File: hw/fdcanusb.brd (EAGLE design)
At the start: 41 x 32 mm, 37 parts, among them J1 MF-CON-MICROUSB-RIGHT, J3 JST-ZH6SMT_VERT, M1 MOUNT, M2 MOUNT, M3 MOUNT, M4 MOUNT, U1 MF-REG-SOT235-3.3V-300mA, U2 USBLC6-2SC6, U3 TCAN334GSOT23, U4 TLP3317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

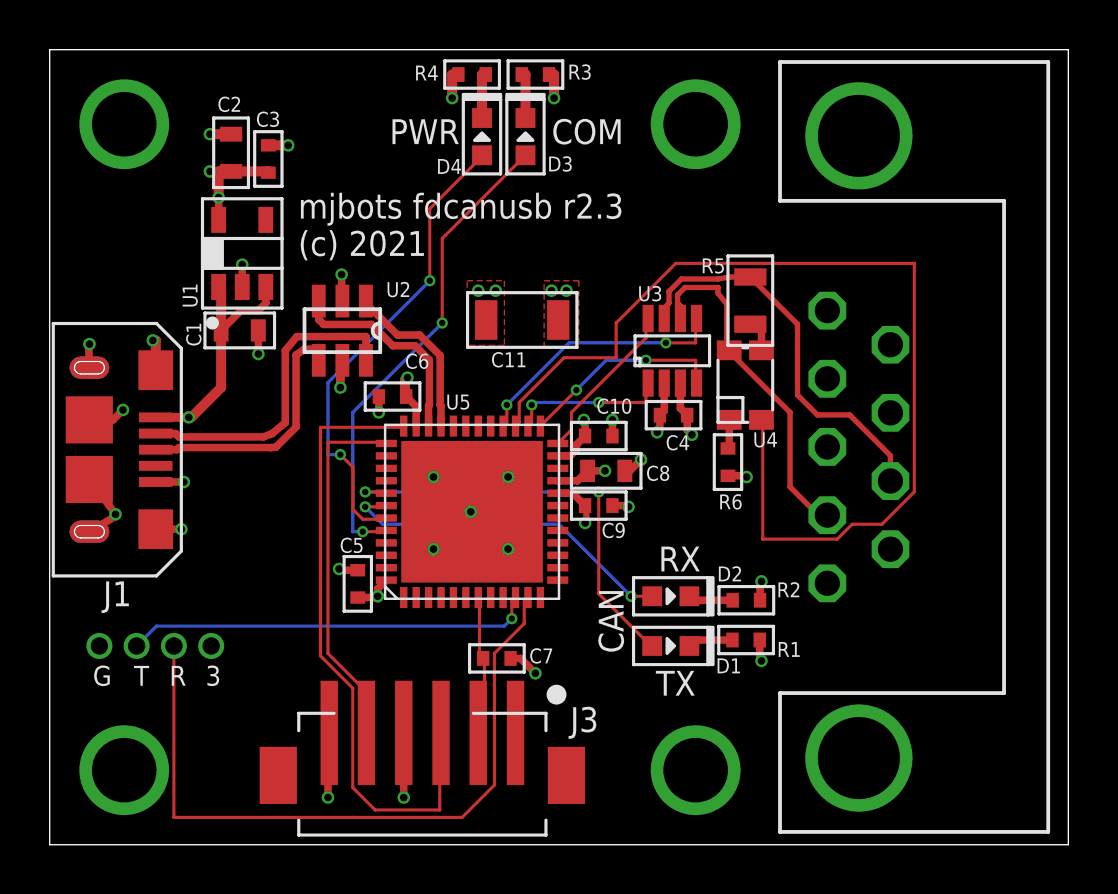
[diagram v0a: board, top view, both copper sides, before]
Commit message: Update PCB to fdcanusb r2.4  * All components are increased to minimum 0603  * Switch to the SOIC package for the CAN transceiver, which is easier    to get  * Switch to 6mil min space/trace
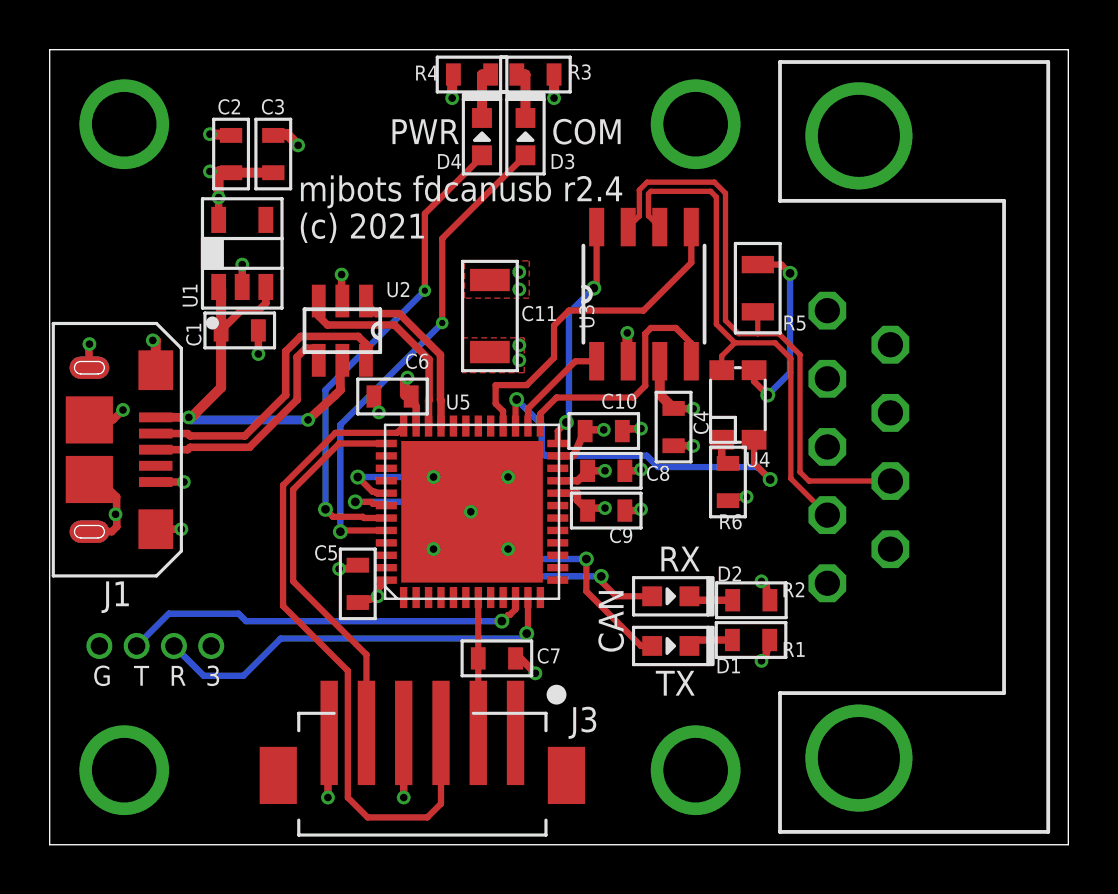
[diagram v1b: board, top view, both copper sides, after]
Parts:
- C10, C3, C4, C5, C6, C7, C9: device mfpassives:C0402 -> mfpassives:C0603
- R1, R2, R3, R4, R6: device mfpassives:R0402 -> mfpassives:R0603
- R5: value 100 -> 120
- U3: value TCAN334GSOT23 -> TCAN334G; device fdcanusb:SOT23-8 -> fdcanusb:SOIC8
- moved U3 2.55 mm to (23.9, 22.2), turned to 90 degrees
- moved C11 1.31 mm to (17.7, 21.3), turned to 90 degrees
- moved U4 0.85 mm to (27.7, 17.7)
- moved R6 0.80 mm to (27.3, 14.6)
- moved R5 0.58 mm to (28.5, 22.4), turned to 90 degrees
- moved C4 0.48 mm to (25.1, 16.8), turned to 270 degrees
- moved C9 0.36 mm to (22.4, 13.4)
- moved C10 0.28 mm to (22.3, 16.6)
- moved C3 0.28 mm to (9.00, 27.8)
- moved R1 0.20 mm to (28.2, 8.24)
- moved R2 0.20 mm to (28.2, 9.84)
- moved C2 0.05 mm to (7.30, 27.8)
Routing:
- net CAN_TERM: track 41.0 -> 15.1 mm, vias 0 -> 2
- net DEBUG_RX: track 28.4 -> 16.9 mm, vias 0 -> 1
- net CAN_P: track 16.0 -> 23.5 mm
- net CAN_N: track 14.0 -> 21.3 mm
- net N$7: track 1.45 -> 7.95 mm, vias 0 -> 2
- net CAN_SHDN: track 10.5 -> 13.9 mm, vias 2 -> 0
- net CAN_STB: track 6.54 -> 9.36 mm, vias 0 -> 2
- net CAN_TX: track 6.37 -> 4.26 mm, vias 2 -> 0
- net CAN_RX: track 8.29 -> 10.2 mm, vias 2 -> 0
- net +3V3: track 20.8 -> 22.2 mm
- net SWDIO: track 25.4 -> 26.7 mm
- net LED_CAN_RX: track 13.9 -> 15.0 mm
- net USB_D_N: track 12.8 -> 12.0 mm
- net SWCLK: track 14.7 -> 15.5 mm
- net LED_COM: track 19.4 -> 20.1 mm
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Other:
- board text added: "mjbots fdcanusb r2.4 (c) 2021"
- board text removed: "mjbots fdcanusb r2.3 (c) 2021"

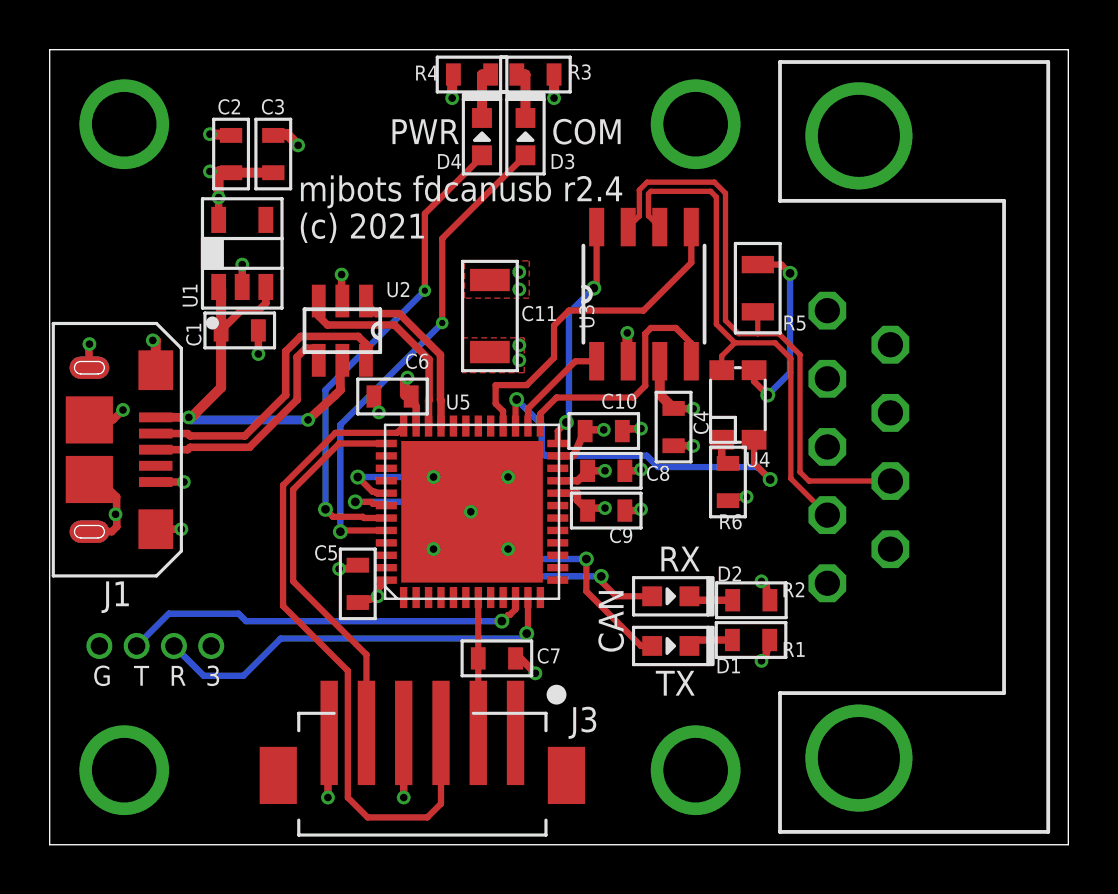
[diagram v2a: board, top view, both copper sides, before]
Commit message: Fine silk placement
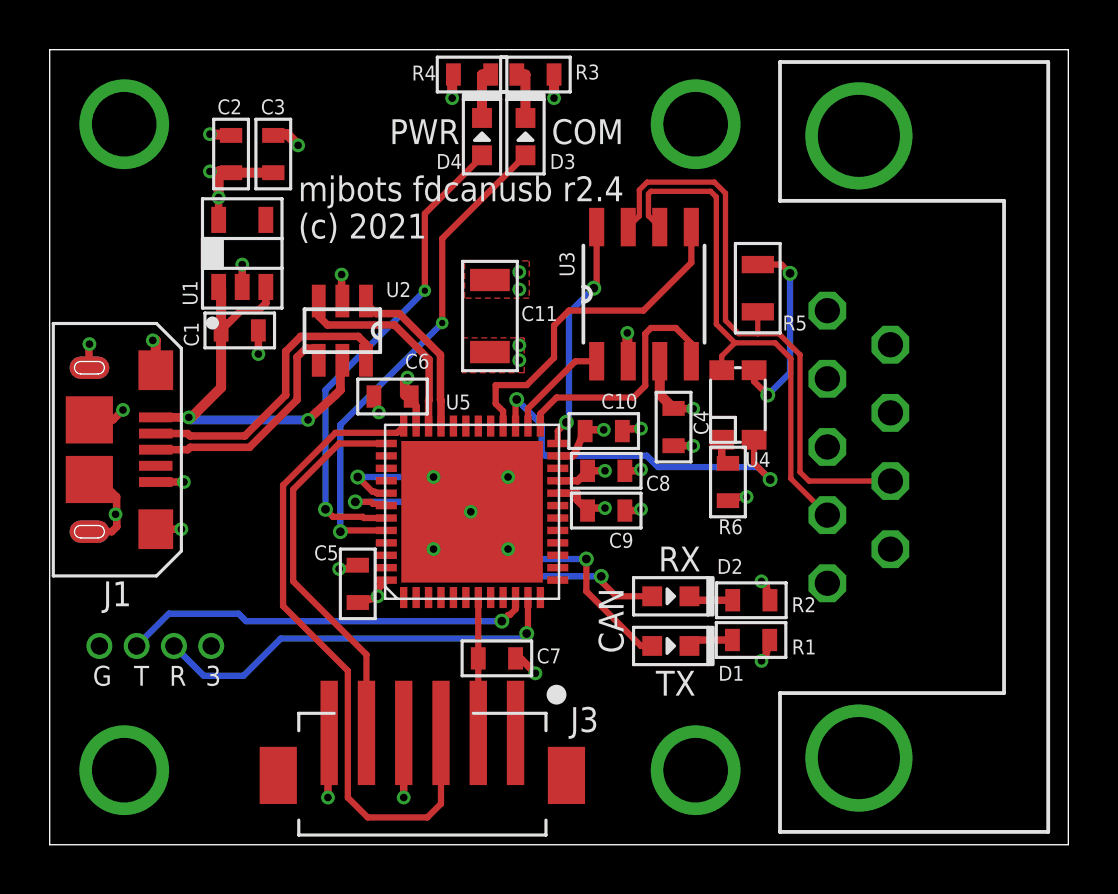
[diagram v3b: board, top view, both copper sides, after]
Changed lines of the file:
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@@
 <attribute name="HOUSEPART" value="YES" x="63.63" y="39.04" size="1.778" layer="27" rot="R90" display="off"/>
 <attribute name="MPN" value="MF-REG-SOT235-3.3V-300mA" x="63.63" y="39.04" size="1.778" layer="27" rot="R90" display="off"/>
-<attribute name="NAME" x="5.95" y="21.6" size="0.6" layer="25" font="vector" ratio="10" rot="R90"/>
+<attribute name="NAME" x="5.95" y="21.7" size="0.6" layer="25" font="vector" ratio="10" rot="R90"/>
 <attribute name="POPULATE" value="1" x="63.63" y="39.04" size="1.778" layer="27" rot="R90" display="off"/>
 <attribute name="URL" value="https://factory.macrofab.com/part/MF-REG-SOT235-3.3V-300mA" x="63.63" y="39.04" size="1.778" layer="27" rot="R90" display="off"/>
@@
 <attribute name="HOUSEPART" value="YES" x="22.89" y="-40.26" size="1.778" layer="27" display="off"/>
 <attribute name="MPN" value="MF-CAP-0603-1uF" x="22.89" y="-40.26" size="1.778" layer="27" display="off"/>
-<attribute name="NAME" x="6.1" y="20.05" size="0.6" layer="25" font="vector" ratio="10" rot="R90"/>
+<attribute name="NAME" x="6" y="20.05" size="0.6" layer="25" font="vector" ratio="10" rot="R90"/>
 <attribute name="POPULATE" value="1" x="22.89" y="-40.26" size="1.778" layer="27" display="off"/>
 <attribute name="TOLERANCE" value="" x="22.89" y="-40.26" size="1.778" layer="27" display="off"/>
@@
 <attribute name="MF" value="TI" x="23.92" y="22.16" size="1.778" layer="27" rot="R90" display="off"/>
 <attribute name="MPN" value="TCAN330GDR" x="23.92" y="22.16" size="1.778" layer="27" rot="R90" display="off"/>
-<attribute name="NAME" x="21.92" y="20.76" size="0.6" layer="25" font="vector" ratio="10" rot="R90"/>
+<attribute name="NAME" x="21.12" y="22.86" size="0.6" layer="25" font="vector" ratio="10" rot="R90"/>
 <attribute name="POPULATE" value="1" x="23.92" y="22.16" size="1.778" layer="27" rot="R90" display="off"/>
 </element>
@@
 <attribute name="HOUSEPART" value="YES" x="68.12" y="-47.51" size="1.778" layer="27" display="off"/>
 <attribute name="MPN" value="MF-CAP-0603-0.1uF" x="68.12" y="-47.51" size="1.778" layer="27" display="off"/>
-<attribute name="NAME" x="23.5" y="12.75" size="0.6" layer="25" font="vector" ratio="10" rot="R180"/>
+<attribute name="NAME" x="23.5" y="12.55" size="0.6" layer="25" font="vector" ratio="10" rot="R180"/>
 <attribute name="POPULATE" value="1" x="68.12" y="-47.51" size="1.778" layer="27" display="off"/>
 <attribute name="TOLERANCE" value="" x="68.12" y="-47.51" size="1.778" layer="27" display="off"/>
@@
 <attribute name="HOUSEPART" value="YES" x="45.26" y="-45.91" size="1.778" layer="27" display="off"/>
 <attribute name="MPN" value="MF-CAP-0603-1uF" x="45.26" y="-45.91" size="1.778" layer="27" display="off"/>
-<attribute name="NAME" x="24" y="14.65" size="0.6" layer="25" font="vector" ratio="10"/>
+<attribute name="NAME" x="24" y="14.25" size="0.6" layer="25" font="vector" ratio="10"/>
 <attribute name="POPULATE" value="1" x="45.26" y="-45.91" size="1.778" layer="27" display="off"/>
 <attribute name="TOLERANCE" value="" x="45.26" y="-45.91" size="1.778" layer="27" display="off"/>
@@
 <attribute name="HOUSEPART" value="YES" x="-13.1" y="62.61" size="1.778" layer="27" rot="R180" display="off"/>
 <attribute name="MPN" value="MF-LED-0603-GREEN" x="-13.1" y="62.61" size="1.778" layer="27" rot="R180" display="off"/>
-<attribute name="NAME" x="26.81" y="6.9" size="0.6" layer="25" font="vector" ratio="10"/>
+<attribute name="NAME" x="26.91" y="6.6" size="0.6" layer="25" font="vector" ratio="10"/>
 <attribute name="POPULATE" value="1" x="-13.1" y="62.61" size="1.778" layer="27" rot="R180" display="off"/>
 <attribute name="URL" value="https://factory.macrofab.com/part/MF-LED-0603-GREEN" x="-13.1" y="62.61" size="1.778" layer="27" rot="R180" display="off"/>
@@
 <attribute name="HOUSEPART" value="YES" x="-20.72" y="64.61" size="1.778" layer="27" rot="R180" display="off"/>
 <attribute name="MPN" value="MF-LED-0603-RED" x="-20.72" y="64.61" size="1.778" layer="27" rot="R180" display="off"/>
-<attribute name="NAME" x="26.86" y="10.6" size="0.6" layer="25" font="vector" ratio="10"/>
+<attribute name="NAME" x="26.86" y="10.9" size="0.6" layer="25" font="vector" ratio="10"/>
 <attribute name="POPULATE" value="1" x="-20.72" y="64.61" size="1.778" layer="27" rot="R180" display="off"/>
 <attribute name="URL" value="https://factory.macrofab.com/part/MF-LED-0603-RED" x="-20.72" y="64.61" size="1.778" layer="27" rot="R180" display="off"/>
@@
 <attribute name="HOUSEPART" value="YES" x="-21.3" y="69.2" size="1.778" layer="27" rot="R180" display="off"/>
 <attribute name="MPN" value="MF-RES-0603-220" x="-21.3" y="69.2" size="1.778" layer="27" rot="R180" display="off"/>
-<attribute name="NAME" x="29.47" y="7.56" size="0.6" layer="25" font="vector" ratio="10"/>
+<attribute name="NAME" x="29.87" y="7.66" size="0.6" layer="25" font="vector" ratio="10"/>
 <attribute name="POPULATE" value="1" x="-21.3" y="69.2" size="1.778" layer="27" rot="R180" display="off"/>
 <attribute name="TOLERANCE" value="" x="-21.3" y="69.2" size="1.778" layer="27" rot="R180" display="off"/>
@@
 <attribute name="HOUSEPART" value="YES" x="-25.1" y="70.8" size="1.778" layer="27" rot="R180" display="off"/>
 <attribute name="MPN" value="MF-RES-0603-220" x="-25.1" y="70.8" size="1.778" layer="27" rot="R180" display="off"/>
-<attribute name="NAME" x="29.46" y="9.96" size="0.6" layer="25" font="vector" ratio="10"/>
+<attribute name="NAME" x="29.86" y="9.36" size="0.6" layer="25" font="vector" ratio="10"/>
 <attribute name="POPULATE" value="1" x="-25.1" y="70.8" size="1.778" layer="27" rot="R180" display="off"/>
 <attribute name="TOLERANCE" value="" x="-25.1" y="70.8" size="1.778" layer="27" rot="R180" display="off"/>
@@
 <attribute name="HOUSEPART" value="YES" x="5.58" y="95.77" size="1.778" layer="27" rot="R180" display="off"/>
 <attribute name="MPN" value="MF-RES-0603-220" x="5.58" y="95.77" size="1.778" layer="27" rot="R180" display="off"/>
-<attribute name="NAME" x="20.85" y="30.8" size="0.6" layer="25" font="vector" ratio="10"/>
+<attribute name="NAME" x="21.15" y="30.8" size="0.6" layer="25" font="vector" ratio="10"/>
 <attribute name="POPULATE" value="1" x="5.58" y="95.77" size="1.778" layer="27" rot="R180" display="off"/>
 <attribute name="TOLERANCE" value="" x="5.58" y="95.77" size="1.778" layer="27" rot="R180" display="off"/>
@@
 <attribute name="HOUSEPART" value="YES" x="34.78" y="-33.77" size="1.778" layer="27" display="off"/>
 <attribute name="MPN" value="MF-RES-0603-220" x="34.78" y="-33.77" size="1.778" layer="27" display="off"/>
-<attribute name="NAME" x="15.66" y="31.36" size="0.6" layer="25" font="vector" ratio="10" rot="R180"/>
+<attribute name="NAME" x="15.56" y="31.36" size="0.6" layer="25" font="vector" ratio="10" rot="R180"/>
 <attribute name="POPULATE" value="1" x="34.78" y="-33.77" size="1.778" layer="27" display="off"/>
 <attribute name="TOLERANCE" value="" x="34.78" y="-33.77" size="1.778" layer="27" display="off"/>
@@
 </element>
 <element name="R6" library="mfpassives" package="R0603" value="330" x="27.3" y="14.6" smashed="yes" rot="R90">
-<attribute name="HOUSEPART" value="" x="27.3" y="14.6" size="1.778" layer="27" rot="R90" display="off"/>
+<attribute name="HOUSEPART" value="YES" x="27.3" y="14.6" size="1.778" layer="27" rot="R90" display="off"/>
 <attribute name="MPN" value="MF-RES-0603-330" x="27.3" y="14.6" size="1.778" layer="27" rot="R90" display="off"/>
-<attribute name="NAME" x="27.9" y="13.3" size="0.6" layer="25" font="vector" ratio="10" rot="R180"/>
+<attribute name="NAME" x="27.9" y="13.1" size="0.6" layer="25" font="vector" ratio="10" rot="R180"/>
 <attribute name="POPULATE" value="1" x="27.3" y="14.6" size="1.778" layer="27" rot="R90" display="off"/>
 <attribute name="TOLERANCE" value="" x="27.3" y="14.6" size="1.778" layer="27" rot="R90" display="off"/>
